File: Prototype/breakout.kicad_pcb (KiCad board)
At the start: 2 copper layers, 8 parts, among them J2 Conn_02x03_Counter_Clockwise, Q1 BSC026NE2LS5, U1 INA214, U2 bq297xx, U3 LM21215, U4 TPS61088, U5 ADA4891-4

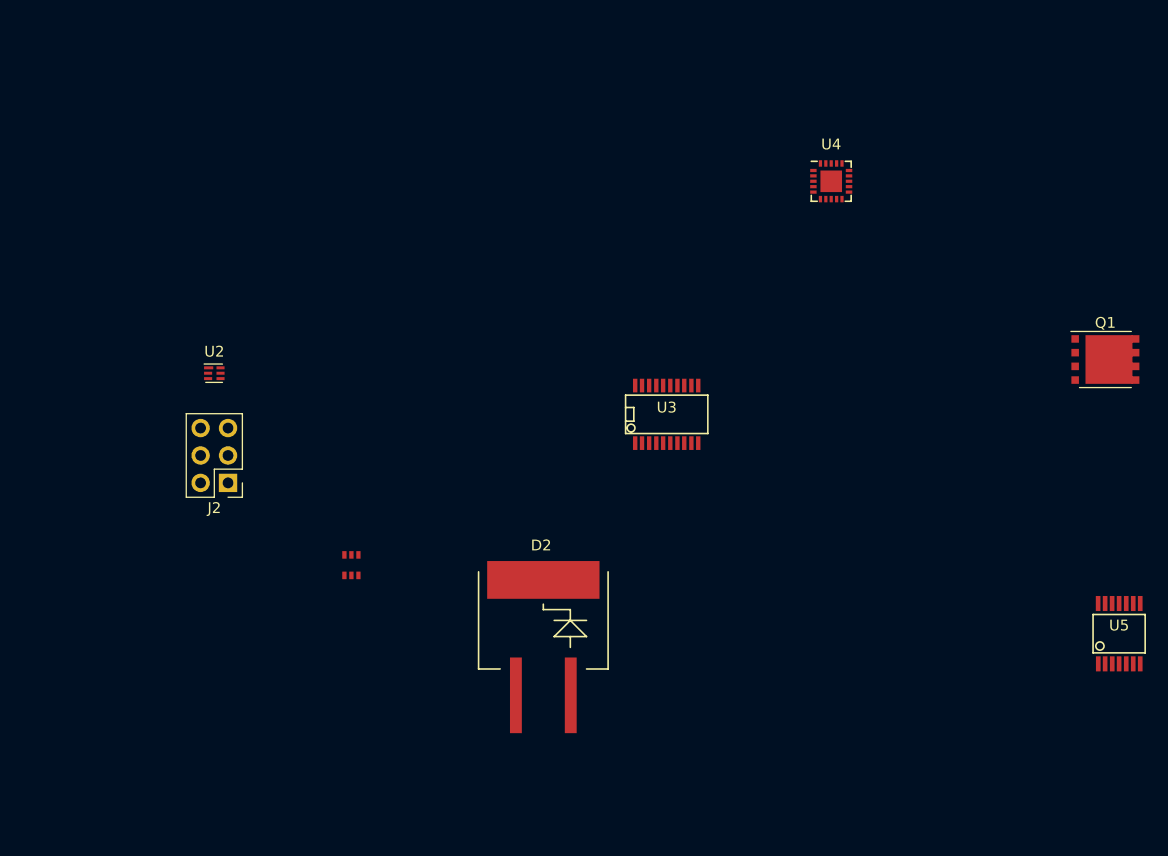
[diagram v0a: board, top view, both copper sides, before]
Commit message: Finished laying out breakout boards
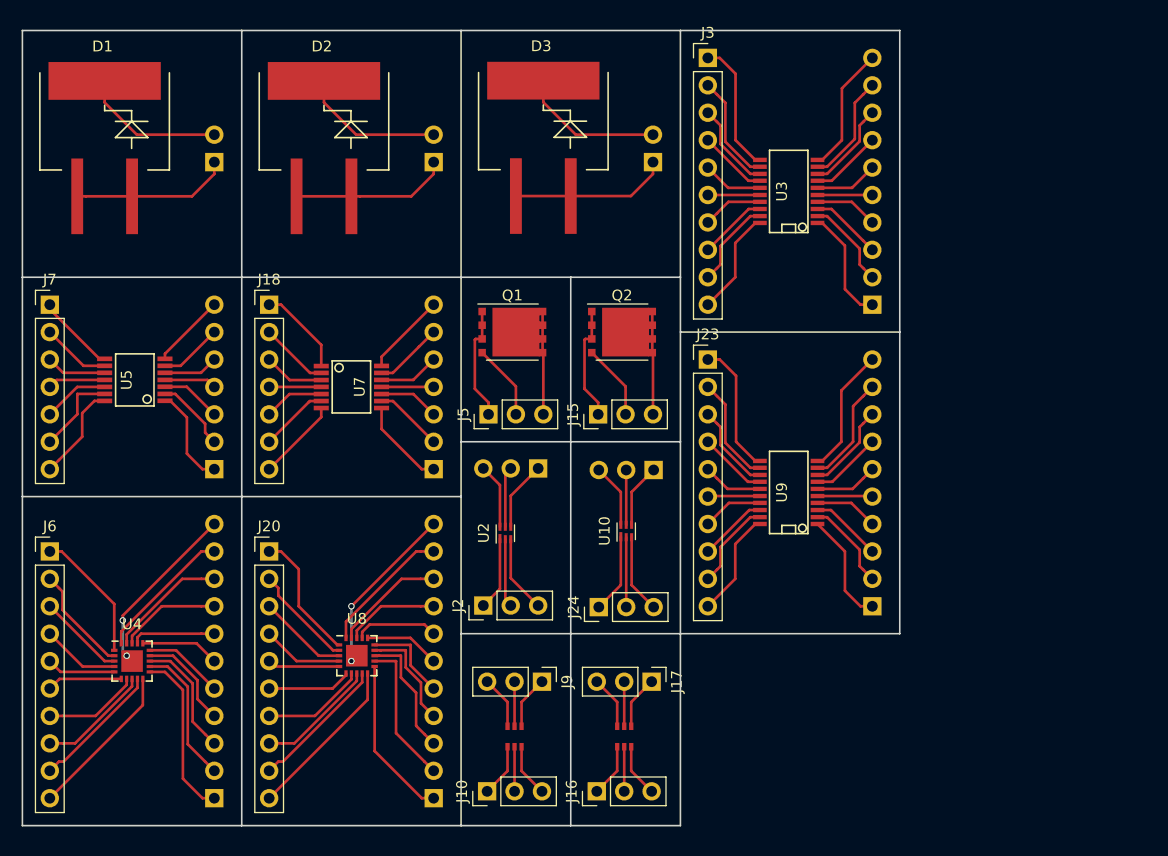
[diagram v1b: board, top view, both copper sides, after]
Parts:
- added D1: SM74611, Diodes_SMD:DD-PAK_TO263_SingleDiode, F.Cu at (20.3, 23.6)
- added D3: SM74611, Diodes_SMD:DD-PAK_TO263_SingleDiode, F.Cu at (61.0, 23.6)
- added J1: Conn_01x10_Male, Pin_Headers:Pin_Header_Straight_1x10_Pitch2.54mm, B.Cu at (91.4, 38.1)
- added J10: Conn_01x03_Male, Pin_Headers:Pin_Header_Straight_1x03_Pitch2.54mm, F.Cu at (55.8, 83.2)
- added J11: Conn_01x03_Male, Pin_Headers:Pin_Header_Straight_1x03_Pitch2.54mm, B.Cu at (60.5, 53.3)
- added J12: Conn_01x02_Male, Pin_Headers:Pin_Header_Straight_1x02_Pitch2.54mm, B.Cu at (50.8, 24.9)
- added J13: Conn_01x02_Male, Pin_Headers:Pin_Header_Straight_1x02_Pitch2.54mm, B.Cu at (30.5, 24.9)
- added J14: Conn_01x02_Male, Pin_Headers:Pin_Header_Straight_1x02_Pitch2.54mm, B.Cu at (71.1, 24.9)
- added J15: Conn_01x03_Male, Pin_Headers:Pin_Header_Straight_1x03_Pitch2.54mm, F.Cu at (66.0, 48.3)
- added J16: Conn_01x03_Male, Pin_Headers:Pin_Header_Straight_1x03_Pitch2.54mm, F.Cu at (65.9, 83.2)
- added J17: Conn_01x03_Male, Pin_Headers:Pin_Header_Straight_1x03_Pitch2.54mm, F.Cu at (71.0, 73.0)
- added J18: Conn_01x07_Male, Pin_Headers:Pin_Header_Straight_1x07_Pitch2.54mm, F.Cu at (35.6, 38.1)
- added J19: Conn_01x07_Male, Pin_Headers:Pin_Header_Straight_1x07_Pitch2.54mm, B.Cu at (50.8, 53.3)
- added J20: Conn_01x10_Male, Pin_Headers:Pin_Header_Straight_1x10_Pitch2.54mm, F.Cu at (35.6, 61.0)
- added J21: Conn_01x11_Male, Pin_Headers:Pin_Header_Straight_1x11_Pitch2.54mm, B.Cu at (50.8, 83.8)
- added J22: Conn_01x10_Male, Pin_Headers:Pin_Header_Straight_1x10_Pitch2.54mm, B.Cu at (91.4, 66.0)
- added J23: Conn_01x10_Male, Pin_Headers:Pin_Header_Straight_1x10_Pitch2.54mm, F.Cu at (76.2, 43.2)
- added J24: Conn_01x03_Male, Pin_Headers:Pin_Header_Straight_1x03_Pitch2.54mm, F.Cu at (66.1, 66.1)
- added J25: Conn_01x03_Male, Pin_Headers:Pin_Header_Straight_1x03_Pitch2.54mm, B.Cu at (71.2, 53.4)
- added J3: Conn_01x10_Male, Pin_Headers:Pin_Header_Straight_1x10_Pitch2.54mm, F.Cu at (76.2, 15.2)
- added J4: Conn_01x07_Male, Pin_Headers:Pin_Header_Straight_1x07_Pitch2.54mm, B.Cu at (30.5, 53.3)
- added J5: Conn_01x03_Male, Pin_Headers:Pin_Header_Straight_1x03_Pitch2.54mm, F.Cu at (55.9, 48.3)
- added J6: Conn_01x10_Male, Pin_Headers:Pin_Header_Straight_1x10_Pitch2.54mm, F.Cu at (15.2, 61.0)
- added J7: Conn_01x07_Male, Pin_Headers:Pin_Header_Straight_1x07_Pitch2.54mm, F.Cu at (15.2, 38.1)
- added J8: Conn_01x11_Male, Pin_Headers:Pin_Header_Straight_1x11_Pitch2.54mm, B.Cu at (30.5, 83.8)
- added J9: Conn_01x03_Male, Pin_Headers:Pin_Header_Straight_1x03_Pitch2.54mm, F.Cu at (60.8, 73.0)
- added Q2: BSC026NE2LS5, Housings_SON:VSONP-8-1EP_5x6_Pitch1.27mm, F.Cu at (68.2, 40.6)
- added U10: bq297xx, Housings_SON:WSON6_1.5x1.5mm_Pitch0.5mm, F.Cu at (68.6, 59.1)
- added U6: INA214, kicad-libraries:SC70-6, F.Cu at (68.5, 78.1)
- added U7: ADA4891-4, SMD_Packages:SSOP-14, F.Cu at (43.2, 45.7)
- added U8: TPS61088, Housings_DFN_QFN:Texas_VQFN-RGR-20, F.Cu at (43.7, 70.6)
- added U9: LM21215, SMD_Packages:SSOP-20, F.Cu at (83.7, 55.5)
- J2: value Conn_02x03_Counter_Clockwise -> Conn_01x03_Male; footprint Pin_Headers:Pin_Header_Straight_2x03_Pitch2.54mm -> Pin_Headers:Pin_Header_Straight_1x03_Pitch2.54mm
- moved U5 94.2 mm to (23.1, 45.1), turned to 90 degrees
- moved U4 78.6 mm to (22.9, 71.1)
- moved Q1 55.0 mm to (58.1, 40.6)
- moved D2 50.5 mm to (40.6, 23.6)
- moved U2 30.8 mm to (57.4, 59.3), turned to 90 degrees
- moved J2 26.2 mm to (55.4, 66.0), turned to 90 degrees
- moved U3 23.5 mm to (83.7, 27.6), turned to 90 degrees
- moved U1 21.9 mm to (58.3, 78.1), turned to 180 degrees
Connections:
- D2 pad 3: Net-(D2-Pad3) -> Net-(D2-Pad1)
- U2 pad 3: Net-(U2-Pad3) -> Net-(J2-Pad3)
- U2 pad 4: Net-(J2-Pad4) -> Net-(J11-Pad1)
- U2 pad 5: Net-(J2-Pad5) -> Net-(J11-Pad2)
- U2 pad 6: Net-(J2-Pad6) -> Net-(J11-Pad3)
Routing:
- net Net-(J8-Pad11): track 0.00 -> 18.9 mm, vias 0 -> 2
- net Net-(J21-Pad11): track 0.00 -> 18.9 mm, vias 0 -> 2
- net Net-(J8-Pad1): track 0.00 -> 15.6 mm
- net Net-(J20-Pad10): track 0.00 -> 15.3 mm
- net Net-(J21-Pad1): track 0.00 -> 15.1 mm
- net Net-(D1-Pad1): track 0.00 -> 14.7 mm
- net Net-(D2-Pad1): track 0.00 -> 14.7 mm
- net Net-(D3-Pad1): track 0.00 -> 14.6 mm
- net Net-(J6-Pad10): track 0.00 -> 14.6 mm
- net Net-(J21-Pad2): track 0.00 -> 13.6 mm
- net Net-(D3-Pad2): track 0.00 -> 13.4 mm
- net Net-(D1-Pad2): track 0.00 -> 13.4 mm
- net Net-(D2-Pad2): track 0.00 -> 13.4 mm
- net Net-(J8-Pad2): track 0.00 -> 13.1 mm
- net Net-(J20-Pad9): track 0.00 -> 12.8 mm
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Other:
- board outline added: 81.3 x 73.7 mm

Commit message: Changed footprint of TPS61088
Also added a dot beside pin 1 of INA214
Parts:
- J1, J8: moved to F.Cu
- J3, J6: moved to B.Cu
- U4, U8: footprint Housings_DFN_QFN:Texas_VQFN-RGR-20 -> w_smd_qfn:pvqfn-n20
- moved J3 27.5 mm to (91.4, 38.1)
- moved J1 27.5 mm to (76.2, 15.2)
- moved U8 21.4 mm to (22.3, 72.7), turned to 270 degrees
- moved J8 20.3 mm to (50.8, 83.8), turned to 180 degrees
- moved J6 20.3 mm to (35.6, 61.0), turned to 180 degrees
- moved J21 20.3 mm to (30.5, 83.8)
- moved J20 20.3 mm to (15.2, 61.0)
- moved U4 20.1 mm to (42.9, 71.9), turned to 270 degrees
- moved U9 1.04 mm to (84.1, 54.5)
- moved U3 0.84 mm to (83.4, 26.8), turned to 270 degrees
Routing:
- net Net-(J21-Pad2): track 13.6 -> 9.54 mm
- net Net-(J20-Pad10): track 15.3 -> 11.6 mm
- net Net-(J20-Pad8): track 11.2 -> 7.47 mm
- net Net-(J20-Pad9): track 12.8 -> 9.11 mm
- net Net-(J21-Pad3): track 11.8 -> 8.44 mm
- net Net-(J20-Pad7): track 9.57 -> 6.56 mm
- net Net-(J8-Pad2): track 13.1 -> 10.4 mm
- net Net-(J8-Pad3): track 11.2 -> 8.59 mm
- net Net-(J21-Pad4): track 10.0 -> 7.60 mm
- net Net-(J21-Pad1): track 15.1 -> 12.7 mm
- net Net-(J21-Pad11): track 18.9 -> 21.3 mm, vias 2 -> 0
- net Net-(J6-Pad10): track 14.6 -> 12.5 mm
- net Net-(J6-Pad8): track 10.5 -> 8.36 mm
- net Net-(J20-Pad6): track 7.78 -> 5.71 mm
- net Net-(J8-Pad11): track 18.9 -> 20.9 mm, vias 2 -> 0
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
